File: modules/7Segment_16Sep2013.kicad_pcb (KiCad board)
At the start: 2 copper layers, 6 parts

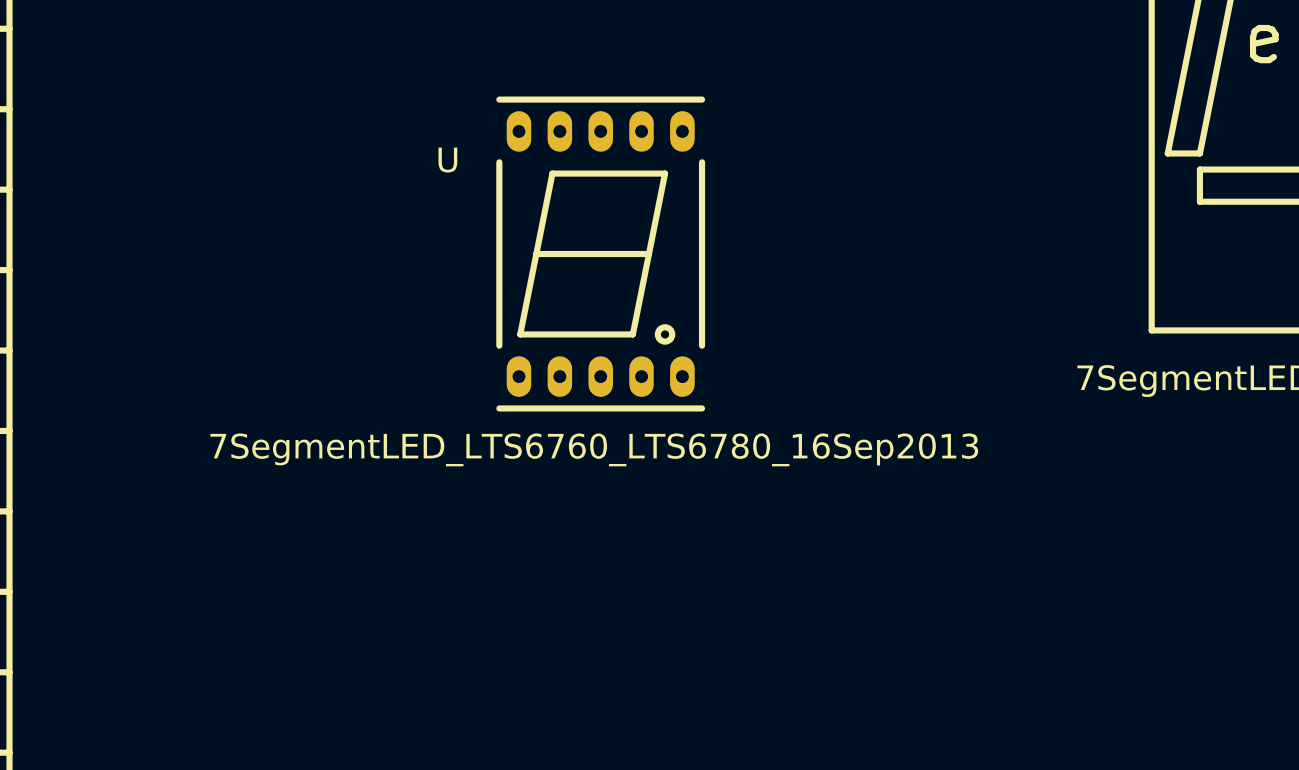
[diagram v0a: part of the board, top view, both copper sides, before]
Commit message: 3D Models for 7 Segment HDSM531/HDSM533 addet
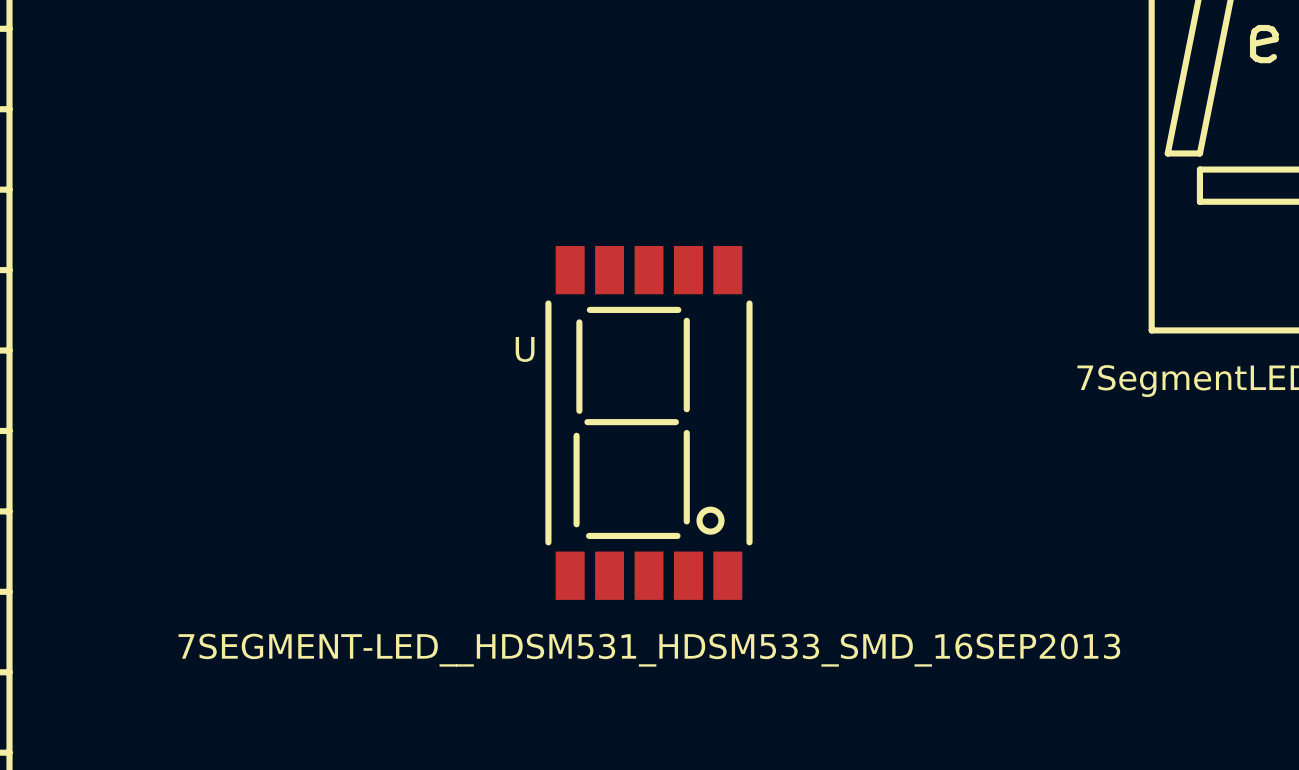
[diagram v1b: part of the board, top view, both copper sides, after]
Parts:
- removed the U at (122.8, 77.0)
- added U: 7SEGMENT-LED__HDSM531_HDSM533_SMD_16SEP2013, 7SEGMENT-LED__HDSM531_HDSM533_SMD_16SEP2013, F.Cu at (125.8, 87.5)
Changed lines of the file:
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@@
     (fp_circle (center 0 0) (end 5.588 0) (layer F.SilkS) (width 0.381))
   )
-  (module 7SegmentLED_LTS6760_LTS6780_16Sep2013 (layer Vorderseite)
-    (at 122.75 77)
-    (fp_text reference U (at -9.5 -5.8) (layer F.SilkS)
+  (module 7SEGMENT-LED__HDSM531_HDSM533_SMD_16SEP2013 (layer Vorderseite)
+    (at 125.75 87.5)
+    (fp_text reference U (at -7.7 -4.525) (layer F.SilkS)
       (effects (font (size 1.524 1.524) (thickness 0.3048)))
     )
-    (fp_text value 7SegmentLED_LTS6760_LTS6780_16Sep2013 (at -0.4 12) (layer F.SilkS)
+    (fp_text value 7SEGMENT-LED__HDSM531_HDSM533_SMD_16SEP2013 (at 0.025 13.95) (layer F.SilkS)
       (effects (font (size 1.524 1.524) (thickness 0.3048)))
     )
-    (fp_circle (center 4 5) (end 4.4 5.2) (layer F.SilkS) (width 0.381))
-    (fp_line (start -3 -5) (end -4 0) (layer F.SilkS) (width 0.381))
-    (fp_line (start -4 0) (end -5 5) (layer F.SilkS) (width 0.381))
-    (fp_line (start -5 5) (end 2 5) (layer F.SilkS) (width 0.381))
-    (fp_line (start 2 5) (end 3 0) (layer F.SilkS) (width 0.381))
-    (fp_line (start 4 -5) (end 3 0) (layer F.SilkS) (width 0.381))
-    (fp_line (start 3 0) (end -4 0) (layer F.SilkS) (width 0.381))
-    (fp_line (start -3 -5) (end 4 -5) (layer F.SilkS) (width 0.381))
-    (fp_line (start 6.3 9.6) (end -6.3 9.6) (layer F.SilkS) (width 0.381))
-    (fp_line (start -6.3 -5.7) (end -6.3 5.7) (layer F.SilkS) (width 0.381))
-    (fp_line (start 6.3 -5.7) (end 6.3 5.7) (layer F.SilkS) (width 0.381))
-    (fp_line (start -6.3 -9.6) (end 6.3 -9.6) (layer F.SilkS) (width 0.381))
-    (pad 1 thru_hole oval (at -5.08 7.62) (size 1.524 2.524) (drill 0.8)
-      (layers *.Cu *.Mask F.SilkS)
+    (fp_circle (center 3.825 6.075) (end 3.925 6.75) (layer F.SilkS) (width 0.381))
+    (fp_line (start 2.35 6.125) (end 2.35 0.625) (layer F.SilkS) (width 0.381))
+    (fp_line (start -4.5 6.3) (end -4.5 0.8) (layer F.SilkS) (width 0.381))
+    (fp_line (start -4.325 -0.75) (end -4.325 -6.25) (layer F.SilkS) (width 0.381))
+    (fp_line (start 2.35 -0.85) (end 2.35 -6.35) (layer F.SilkS) (width 0.381))
+    (fp_line (start -3.675 -7.025) (end 1.825 -7.025) (layer F.SilkS) (width 0.381))
+    (fp_line (start -3.825 -0.05) (end 1.675 -0.05) (layer F.SilkS) (width 0.381))
+    (fp_line (start -3.725 7.025) (end 1.775 7.025) (layer F.SilkS) (width 0.381))
+    (fp_line (start 6.25 7.425) (end 6.25 -7.425) (layer F.SilkS) (width 0.381))
+    (fp_line (start -6.25 -7.425) (end -6.25 7.425) (layer F.SilkS) (width 0.381))
+    (pad 3 smd rect (at 0 9.5) (size 1.8 3)
+      (layers Vorderseite F.Paste F.Mask)
     )
-    (pad 2 thru_hole oval (at -2.54 7.62) (size 1.524 2.524) (drill 0.8)
-      (layers *.Cu *.Mask F.SilkS)
+    (pad 2 smd rect (at -2.45 9.5) (size 1.8 3)
+      (layers Vorderseite F.Paste F.Mask)
     )
-    (pad 3 thru_hole oval (at 0 7.62) (size 1.524 2.524) (drill 0.8)
-      (layers *.Cu *.Mask F.SilkS)
+    (pad 1 smd rect (at -4.9 9.5) (size 1.8 3)
+      (layers Vorderseite F.Paste F.Mask)
     )
-    (pad 4 thru_hole oval (at 2.54 7.62) (size 1.524 2.524) (drill 0.8)
-      (layers *.Cu *.Mask F.SilkS)
+    (pad 4 smd rect (at 2.45 9.5) (size 1.8 3)
+      (layers Vorderseite F.Paste F.Mask)
     )
-    (pad 5 thru_hole oval (at 5.08 7.62) (size 1.524 2.524) (drill 0.8)
-      (layers *.Cu *.Mask F.SilkS)
+    (pad 5 smd rect (at 4.9 9.5) (size 1.8 3)
+      (layers Vorderseite F.Paste F.Mask)
     )
-    (pad 6 thru_hole oval (at 5.08 -7.62) (size 1.524 2.524) (drill 0.8)
-      (layers *.Cu *.Mask F.SilkS)
+    (pad 6 smd rect (at 4.9 -9.5) (size 1.8 3)
+      (layers Vorderseite F.Paste F.Mask)
     )
-    (pad 7 thru_hole oval (at 2.54 -7.62) (size 1.524 2.524) (drill 0.8)
-      (layers *.Cu *.Mask F.SilkS)
+    (pad 7 smd rect (at 2.45 -9.5) (size 1.8 3)
+      (layers Vorderseite F.Paste F.Mask)
     )
-    (pad 8 thru_hole oval (at 0 -7.62) (size 1.524 2.524) (drill 0.8)
-      (layers *.Cu *.Mask F.SilkS)
+    (pad 8 smd rect (at 0 -9.5) (size 1.8 3)
+      (layers Vorderseite F.Paste F.Mask)
     )
-    (pad 9 thru_hole oval (at -2.54 -7.62) (size 1.524 2.524) (drill 0.8)
-      (layers *.Cu *.Mask F.SilkS)
+    (pad 9 smd rect (at -2.45 -9.5) (size 1.8 3)
+      (layers Vorderseite F.Paste F.Mask)
     )
-    (pad 10 thru_hole oval (at -5.08 -7.62) (size 1.524 2.524) (drill 0.8)
-      (layers *.Cu *.Mask F.SilkS)
+    (pad 10 smd rect (at -4.9 -9.5) (size 1.8 3)
+      (layers Vorderseite F.Paste F.Mask)
+    )
+    (pad "" smd oval (at 0 0) (size 4 6)
+      (layers F.Adhes)
+    )
+    (model 7Segment_HDSM531_HDSM533_Wings3D_RevA_17Sep2013/7Segment_HDSM531_HDSM533_Green_Faktor03937_Wings3D_RevA_17Sep2013.wrl
+      (at (xyz 0 0 0))
+      (scale (xyz 0.3937 0.3937 0.3937))
+      (rotate (xyz 0 0 0))
     )
   )

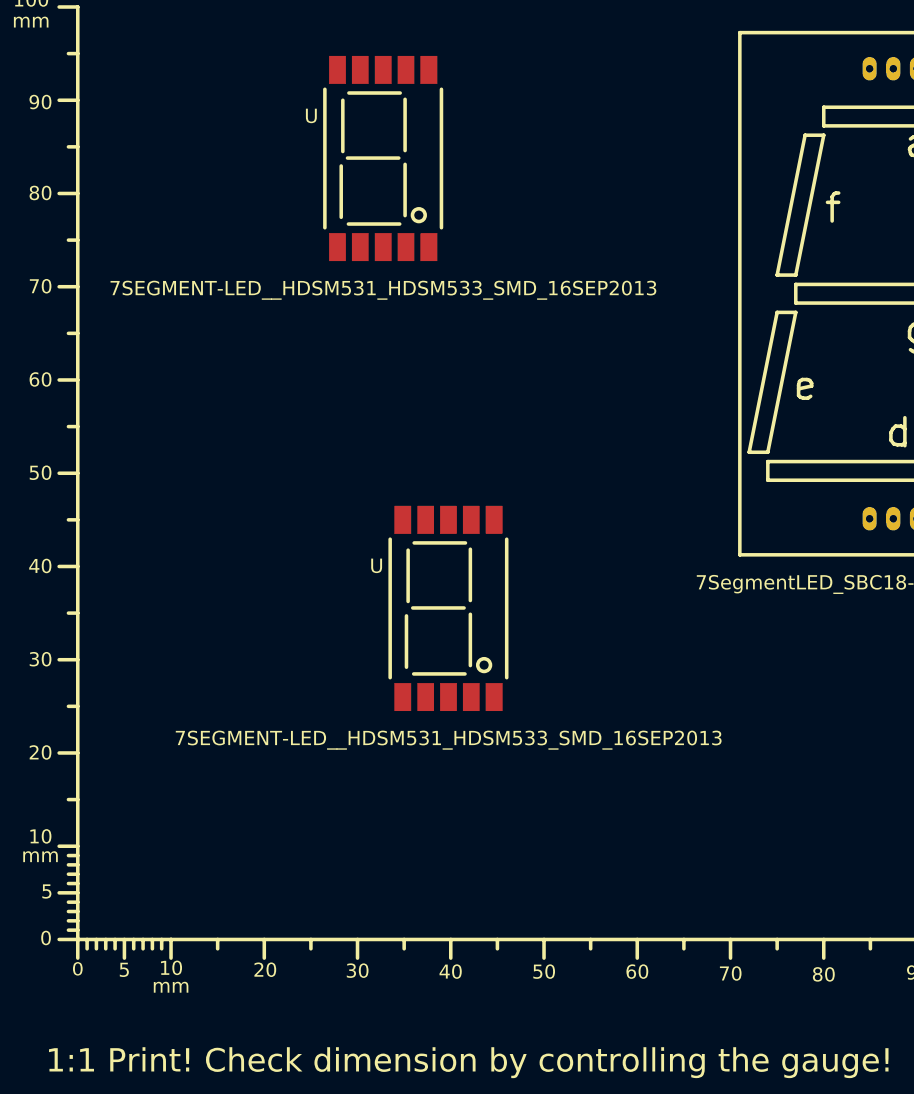
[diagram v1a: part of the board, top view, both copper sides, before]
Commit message: Changing buildinglocks line endings to Unix type
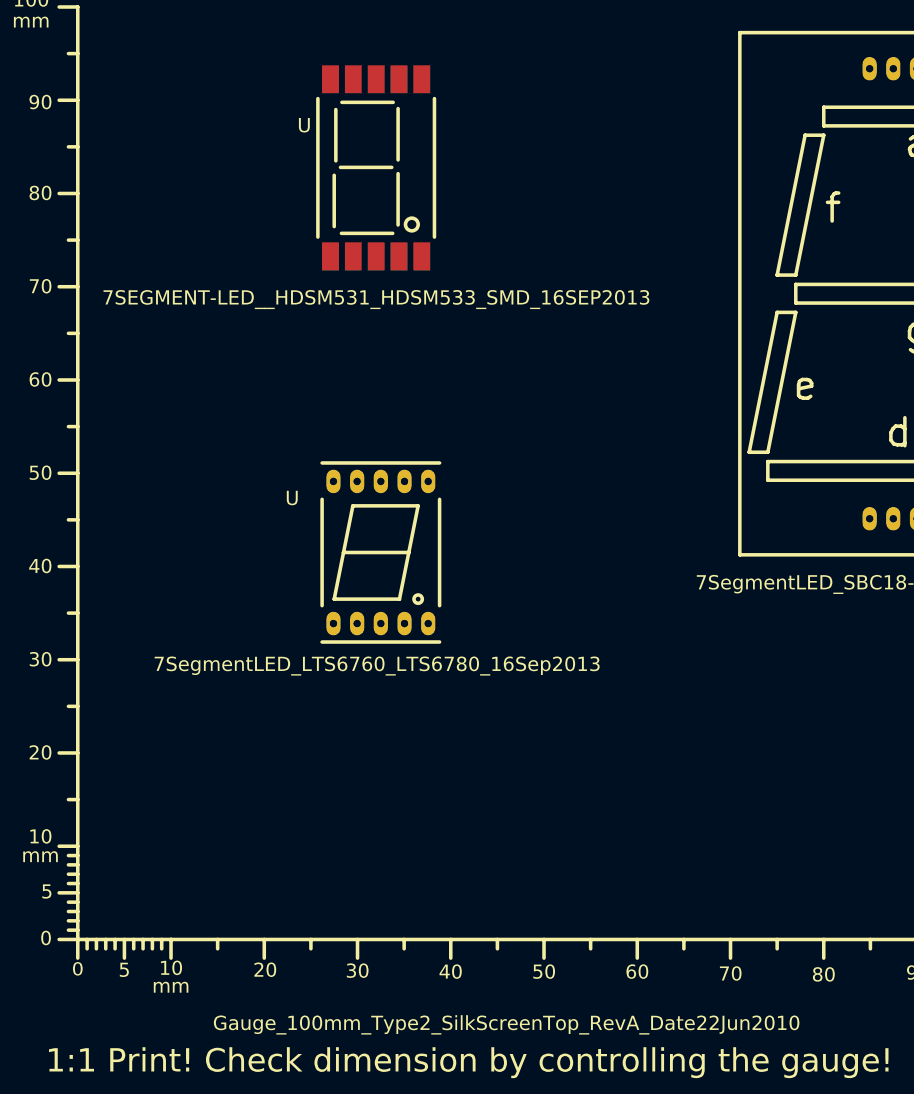
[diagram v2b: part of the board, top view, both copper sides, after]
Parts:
- removed the U at (118.8, 39.2)
- removed the U at (125.8, 87.5)
- added U: 7SegmentLED_LTS6760_LTS6780_16Sep2013, 7SegmentLED_LTS6760_LTS6780_16Sep2013, F.Cu at (118.5, 81.5)
- added U: 7SEGMENT-LED__HDSM531_HDSM533_SMD_16SEP2013, 7SEGMENT-LED__HDSM531_HDSM533_SMD_16SEP2013, F.Cu at (118.0, 40.2)
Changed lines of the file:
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@@
     (mod_text_size 1.524 1.524)
     (mod_text_width 0.3048)
-    (pad_size 1.524 1.524)
-    (pad_drill 0.8128)
+    (pad_size 1.8 3)
+    (pad_drill 0)
     (pad_to_mask_clearance 0.254)
     (aux_axis_origin 0 0)
@@
     (uvia_drill 0.127)
     (add_net "")
-  )
-  (module 7SEGMENT-LED__HDSM531_HDSM533_SMD_16SEP2013 (layer Vorderseite)
-    (at 118.75 39.25)
-    (fp_text reference U (at -7.7 -4.525) (layer F.SilkS)
-      (effects (font (size 1.524 1.524) (thickness 0.3048)))
-    )
-    (fp_text value 7SEGMENT-LED__HDSM531_HDSM533_SMD_16SEP2013 (at 0.025 13.95) (layer F.SilkS)
-      (effects (font (size 1.524 1.524) (thickness 0.3048)))
-    )
-    (fp_circle (center 3.825 6.075) (end 3.925 6.75) (layer F.SilkS) (width 0.381))
-    (fp_line (start 2.35 6.125) (end 2.35 0.625) (layer F.SilkS) (width 0.381))
-    (fp_line (start -4.5 6.3) (end -4.5 0.8) (layer F.SilkS) (width 0.381))
-    (fp_line (start -4.325 -0.75) (end -4.325 -6.25) (layer F.SilkS) (width 0.381))
-    (fp_line (start 2.35 -0.85) (end 2.35 -6.35) (layer F.SilkS) (width 0.381))
-    (fp_line (start -3.675 -7.025) (end 1.825 -7.025) (layer F.SilkS) (width 0.381))
-    (fp_line (start -3.825 -0.05) (end 1.675 -0.05) (layer F.SilkS) (width 0.381))
-    (fp_line (start -3.725 7.025) (end 1.775 7.025) (layer F.SilkS) (width 0.381))
-    (fp_line (start 6.25 7.425) (end 6.25 -7.425) (layer F.SilkS) (width 0.381))
-    (fp_line (start -6.25 -7.425) (end -6.25 7.425) (layer F.SilkS) (width 0.381))
-    (pad 3 smd rect (at 0 9.5) (size 1.8 3)
-      (layers Vorderseite F.Paste F.Mask)
-    )
-    (pad 2 smd rect (at -2.45 9.5) (size 1.8 3)
-      (layers Vorderseite F.Paste F.Mask)
-    )
-    (pad 1 smd rect (at -4.9 9.5) (size 1.8 3)
-      (layers Vorderseite F.Paste F.Mask)
-    )
-    (pad 4 smd rect (at 2.45 9.5) (size 1.8 3)
-      (layers Vorderseite F.Paste F.Mask)
-    )
-    (pad 5 smd rect (at 4.9 9.5) (size 1.8 3)
-      (layers Vorderseite F.Paste F.Mask)
-    )
-    (pad 6 smd rect (at 4.9 -9.5) (size 1.8 3)
-      (layers Vorderseite F.Paste F.Mask)
-    )
-    (pad 7 smd rect (at 2.45 -9.5) (size 1.8 3)
-      (layers Vorderseite F.Paste F.Mask)
-    )
-    (pad 8 smd rect (at 0 -9.5) (size 1.8 3)
-      (layers Vorderseite F.Paste F.Mask)
-    )
-    (pad 9 smd rect (at -2.45 -9.5) (size 1.8 3)
-      (layers Vorderseite F.Paste F.Mask)
-    )
-    (pad 10 smd rect (at -4.9 -9.5) (size 1.8 3)
-      (layers Vorderseite F.Paste F.Mask)
-    )
-    (pad "" smd oval (at 0 0) (size 4 6)
-      (layers F.Adhes)
-    )
   )
   (module 7SegmentLED_SBC18-11EGWA_16Sep2013 (layer Vorderseite)
@@
       (effects (font (size 1.524 1.524) (thickness 0.3048)))
     )
-    (fp_text value Gauge_100mm_Type2_SilkScreenTop_RevA_Date22Jun2010 (at 45.9994 8.99922) (layer F.SilkS) hide
+    (fp_text value Gauge_100mm_Type2_SilkScreenTop_RevA_Date22Jun2010 (at 45.9994 8.99922) (layer F.SilkS)
       (effects (font (size 1.524 1.524) (thickness 0.3048)))
     )
@@
     (fp_circle (center 0 0) (end 5.588 0) (layer F.SilkS) (width 0.381))
   )
+  (module 7SegmentLED_LTS6760_LTS6780_16Sep2013 (layer Vorderseite)
+    (at 118.5 81.5)
+    (fp_text reference U (at -9.5 -5.8) (layer F.SilkS)
+      (effects (font (size 1.524 1.524) (thickness 0.3048)))
+    )
+    (fp_text value 7SegmentLED_LTS6760_LTS6780_16Sep2013 (at -0.4 12) (layer F.SilkS)
+      (effects (font (size 1.524 1.524) (thickness 0.3048)))
+    )
+    (fp_circle (center 4 5) (end 4.4 5.2) (layer F.SilkS) (width 0.381))
+    (fp_line (start -3 -5) (end -4 0) (layer F.SilkS) (width 0.381))
+    (fp_line (start -4 0) (end -5 5) (layer F.SilkS) (width 0.381))
+    (fp_line (start -5 5) (end 2 5) (layer F.SilkS) (width 0.381))
+    (fp_line (start 2 5) (end 3 0) (layer F.SilkS) (width 0.381))
+    (fp_line (start 4 -5) (end 3 0) (layer F.SilkS) (width 0.381))
+    (fp_line (start 3 0) (end -4 0) (layer F.SilkS) (width 0.381))
+    (fp_line (start -3 -5) (end 4 -5) (layer F.SilkS) (width 0.381))
+    (fp_line (start 6.3 9.6) (end -6.3 9.6) (layer F.SilkS) (width 0.381))
+    (fp_line (start -6.3 -5.7) (end -6.3 5.7) (layer F.SilkS) (width 0.381))
+    (fp_line (start 6.3 -5.7) (end 6.3 5.7) (layer F.SilkS) (width 0.381))
+    (fp_line (start -6.3 -9.6) (end 6.3 -9.6) (layer F.SilkS) (width 0.381))
+    (pad 1 thru_hole oval (at -5.08 7.62) (size 1.524 2.524) (drill 0.8)
+      (layers *.Cu *.Mask F.SilkS)
+    )
+    (pad 2 thru_hole oval (at -2.54 7.62) (size 1.524 2.524) (drill 0.8)
+      (layers *.Cu *.Mask F.SilkS)
+    )
+    (pad 3 thru_hole oval (at 0 7.62) (size 1.524 2.524) (drill 0.8)
+      (layers *.Cu *.Mask F.SilkS)
+    )
+    (pad 4 thru_hole oval (at 2.54 7.62) (size 1.524 2.524) (drill 0.8)
+      (layers *.Cu *.Mask F.SilkS)
+    )
+    (pad 5 thru_hole oval (at 5.08 7.62) (size 1.524 2.524) (drill 0.8)
+      (layers *.Cu *.Mask F.SilkS)
+    )
+    (pad 6 thru_hole oval (at 5.08 -7.62) (size 1.524 2.524) (drill 0.8)
+      (layers *.Cu *.Mask F.SilkS)
+    )
+    (pad 7 thru_hole oval (at 2.54 -7.62) (size 1.524 2.524) (drill 0.8)
+      (layers *.Cu *.Mask F.SilkS)
+    )
+    (pad 8 thru_hole oval (at 0 -7.62) (size 1.524 2.524) (drill 0.8)
+      (layers *.Cu *.Mask F.SilkS)
+    )
+    (pad 9 thru_hole oval (at -2.54 -7.62) (size 1.524 2.524) (drill 0.8)
+      (layers *.Cu *.Mask F.SilkS)
+    )
+    (pad 10 thru_hole oval (at -5.08 -7.62) (size 1.524 2.524) (drill 0.8)
+      (layers *.Cu *.Mask F.SilkS)
+    )
+  )
   (module 7SEGMENT-LED__HDSM531_HDSM533_SMD_16SEP2013 (layer Vorderseite)
-    (at 125.75 87.5)
+    (at 118 40.25)
     (fp_text reference U (at -7.7 -4.525) (layer F.SilkS)
       (effects (font (size 1.524 1.524) (thickness 0.3048)))
@@
     (pad 3 smd rect (at 0 9.5) (size 1.8 3)
       (layers Vorderseite F.Paste F.Mask)
+      (solder_paste_margin -0.2)
     )
     (pad 2 smd rect (at -2.45 9.5) (size 1.8 3)
       (layers Vorderseite F.Paste F.Mask)
+      (solder_paste_margin -0.2)
     )
     (pad 1 smd rect (at -4.9 9.5) (size 1.8 3)
       (layers Vorderseite F.Paste F.Mask)
+      (solder_paste_margin -0.2)
     )
     (pad 4 smd rect (at 2.45 9.5) (size 1.8 3)
       (layers Vorderseite F.Paste F.Mask)
+      (solder_paste_margin -0.2)
     )
     (pad 5 smd rect (at 4.9 9.5) (size 1.8 3)
       (layers Vorderseite F.Paste F.Mask)
+      (solder_paste_margin -0.2)
     )
     (pad 6 smd rect (at 4.9 -9.5) (size 1.8 3)
       (layers Vorderseite F.Paste F.Mask)
+      (solder_paste_margin -0.2)
     )
     (pad 7 smd rect (at 2.45 -9.5) (size 1.8 3)
       (layers Vorderseite F.Paste F.Mask)
+      (solder_paste_margin -0.2)
     )
     (pad 8 smd rect (at 0 -9.5) (size 1.8 3)
       (layers Vorderseite F.Paste F.Mask)
+      (solder_paste_margin -0.2)
     )
     (pad 9 smd rect (at -2.45 -9.5) (size 1.8 3)
       (layers Vorderseite F.Paste F.Mask)
+      (solder_paste_margin -0.2)
     )
     (pad 10 smd rect (at -4.9 -9.5) (size 1.8 3)
       (layers Vorderseite F.Paste F.Mask)
+      (solder_paste_margin -0.2)
     )
     (pad "" smd oval (at 0 0) (size 4 6)
